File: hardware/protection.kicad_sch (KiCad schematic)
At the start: 13 parts

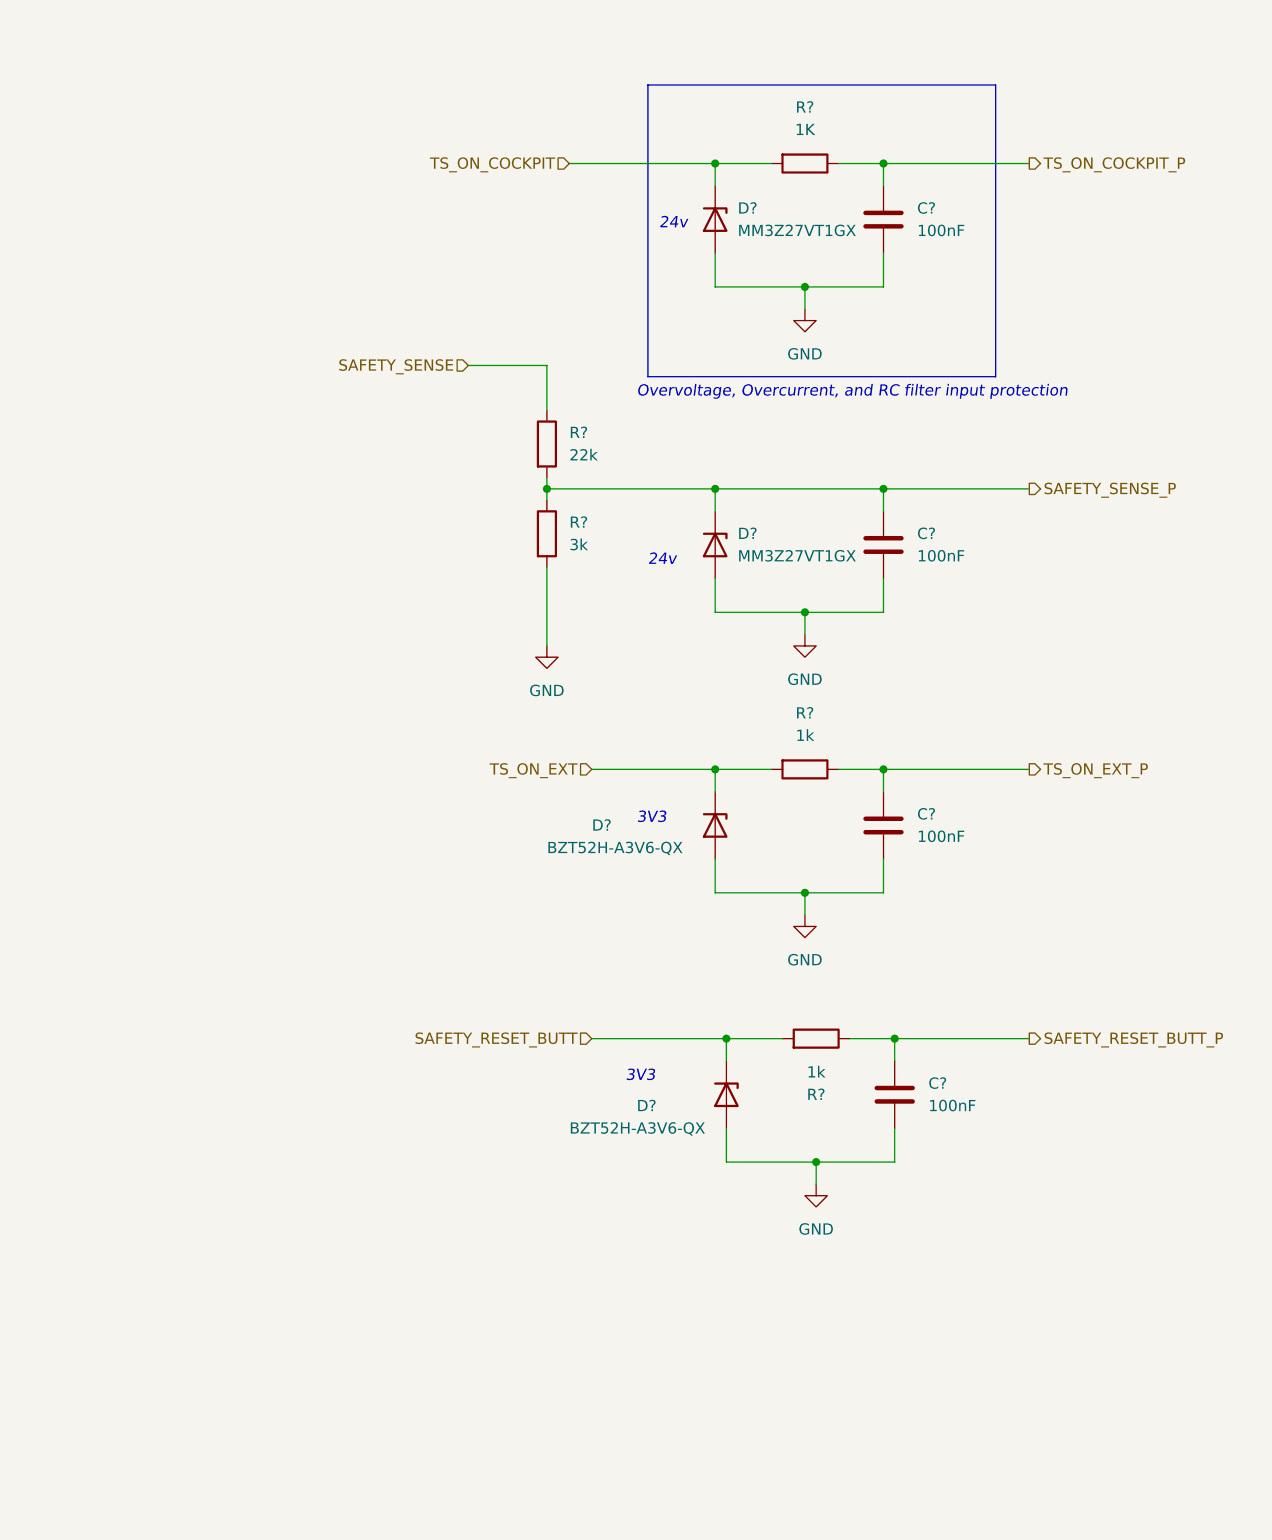
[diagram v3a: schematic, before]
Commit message: Schematic ready for second review
Cleaned up, numerated, added footprints, JW notes considered
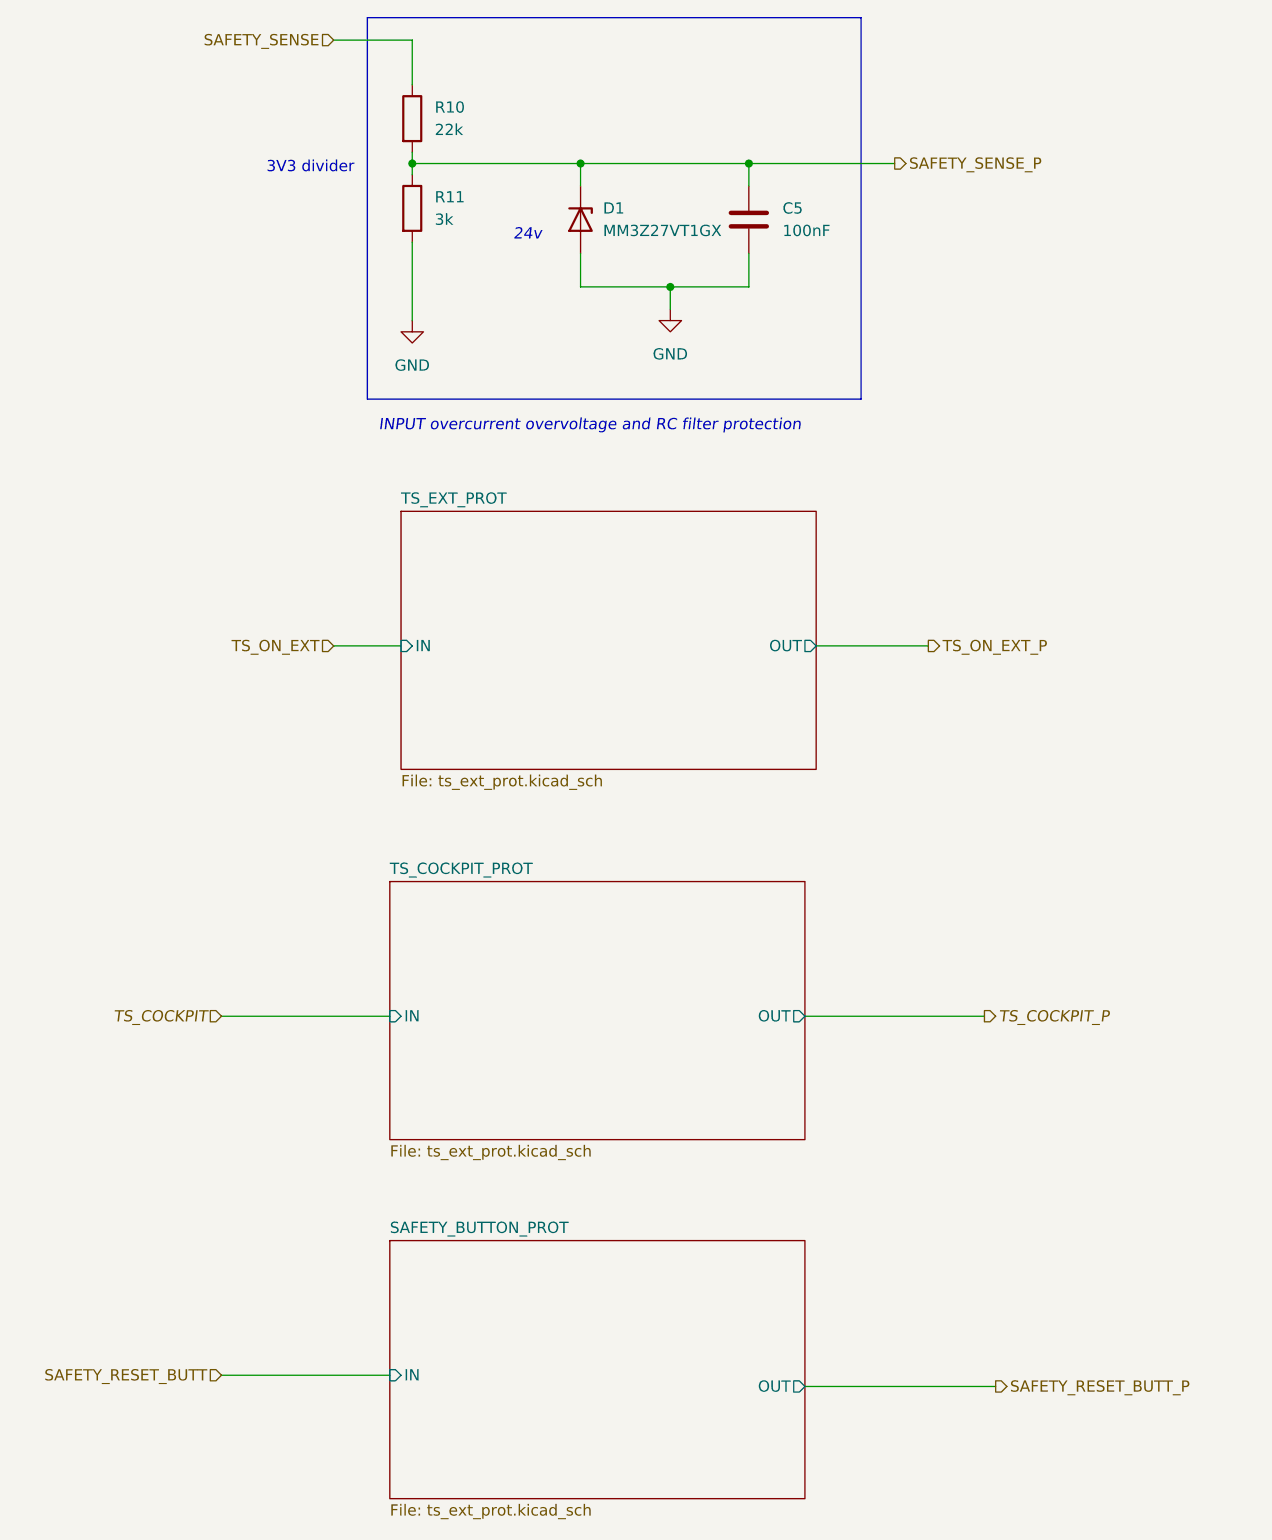
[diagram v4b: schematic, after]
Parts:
- removed C? (x3): 100nF, symbol Device:C
- removed D?: MM3Z27VT1GX, symbol Device:D_Zener
- removed D? (x2): BZT52H-A3V6-QX, symbol Device:D_Zener
- removed R? (x2): 1k, symbol Device:R
- removed R?: 1K, symbol Device:R
- C5: renamed from C?; footprint (none) -> Capacitor_SMD:C_0201_0603Metric_Pad0.64x0.40mm_HandSolder
- R10, R11: renamed from R?; footprint (none) -> Resistor_SMD:R_0603_1608Metric
- gave numbers to parts that had none: 1
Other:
- added sheet SAFETY_BUTTON_PROT (ts_ext_prot.kicad_sch)
- added sheet TS_COCKPIT_PROT (ts_ext_prot.kicad_sch)
- added sheet TS_EXT_PROT (ts_ext_prot.kicad_sch)
- note added: "3V3 divider"
- note added: "INPUT overcurrent overvoltage and RC filter protection"
- note removed: "3V3"
- note removed: "Overvoltage, Overcurrent, and RC filter input protection"
- moved on the sheet: C5, D1, R10, R11

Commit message: 0xERC State
Schematic needs only simulation and veryfying component choice for now
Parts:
- D1: value MM3Z27VT1GX -> BZX38450-C3V3-QX; footprint (none) -> Diode_SMD:D_SOD-323_HandSoldering
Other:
- note removed: "24v"
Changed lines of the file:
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@@
     (effects (font (size 1.27 1.27)) (justify left bottom))
-  )
-  (text "24v\n" (at 91.44 48.26 0)
-    (effects (font (size 1.27 1.27) italic) (justify left bottom))
   )
   (text "INPUT overcurrent overvoltage and RC filter protection"
@@
   )
   (symbol (lib_id "Device:D_Zener") (at 99.06 45.72 270) (unit 1)
-    (in_bom yes) (on_board yes) (fields_autoplaced)
-    (property "Reference" "D1" (id 0) (at 101.6 44.4499 90)
+    (in_bom yes) (on_board yes)
+    (property "Reference" "D1" (id 0) (at 93.98 45.72 90)
       (effects (font (size 1.27 1.27)) (justify left))
     )
-    (property "Value" "MM3Z27VT1GX" (id 1) (at 101.6 46.9899 90)
+    (property "Value" "BZX38450-C3V3-QX" (id 1) (at 88.9 49.53 90)
       (effects (font (size 1.27 1.27)) (justify left))
     )
-    (property "Footprint" "" (id 2) (at 99.06 45.72 0)
+    (property "Footprint" "Diode_SMD:D_SOD-323_HandSoldering" (id 2) (at 99.06 45.72 0)
       (effects (font (size 1.27 1.27)) hide)
     )
-    (property "Datasheet" "~" (id 3) (at 99.06 45.72 0)
+    (property "Datasheet" "https://www.mouser.pl/datasheet/2/916/BZX38450_Q_SER-2580608.pdf" (id 3) (at 99.06 45.72 0)
       (effects (font (size 1.27 1.27)) hide)
     )

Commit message: working simulations, assigned footprints
"nightly" relase
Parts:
- C5: value 100nF -> 10nF
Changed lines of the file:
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@@
       (effects (font (size 1.27 1.27)) (justify left))
     )
-    (property "Value" "100nF" (id 1) (at 121.92 46.9899 0)
+    (property "Value" "10nF" (id 1) (at 121.92 46.9899 0)
       (effects (font (size 1.27 1.27)) (justify left))
     )

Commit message: kończymy balet na dziś
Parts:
- C5: footprint Capacitor_SMD:C_0201_0603Metric_Pad0.64x0.40mm_HandSolder -> Capacitor_SMD:C_0603_1608Metric_Pad1.08x0.95mm_HandSolder
- R10, R11: footprint Resistor_SMD:R_0603_1608Metric -> Resistor_SMD:R_0603_1608Metric_Pad0.98x0.95mm_HandSolder
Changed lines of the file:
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@@
       (effects (font (size 1.27 1.27)) (justify left))
     )
-    (property "Footprint" "Capacitor_SMD:C_0201_0603Metric_Pad0.64x0.40mm_HandSolder" (id 2) (at 119.0752 49.53 0)
+    (property "Footprint" "Capacitor_SMD:C_0603_1608Metric_Pad1.08x0.95mm_HandSolder" (id 2) (at 119.0752 49.53 0)
       (effects (font (size 1.27 1.27)) hide)
     )
@@
       (effects (font (size 1.27 1.27)) (justify left))
     )
-    (property "Footprint" "Resistor_SMD:R_0603_1608Metric" (id 2) (at 78.232 34.29 90)
+    (property "Footprint" "Resistor_SMD:R_0603_1608Metric_Pad0.98x0.95mm_HandSolder" (id 2) (at 78.232 34.29 90)
       (effects (font (size 1.27 1.27)) hide)
     )
@@
       (effects (font (size 1.27 1.27)) (justify left))
     )
-    (property "Footprint" "Resistor_SMD:R_0603_1608Metric" (id 2) (at 78.232 44.45 90)
+    (property "Footprint" "Resistor_SMD:R_0603_1608Metric_Pad0.98x0.95mm_HandSolder" (id 2) (at 78.232 44.45 90)
       (effects (font (size 1.27 1.27)) hide)
     )
